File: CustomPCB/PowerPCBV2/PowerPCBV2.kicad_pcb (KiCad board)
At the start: 2 copper layers, 18 parts, among them J1 XT30, J2 XT60, J3 Barrel_Jack_12V, J4 Barrel_Jack_5V, U1 LM2677T-Fixed-12V, U2 LM2677T-Fixed-5V

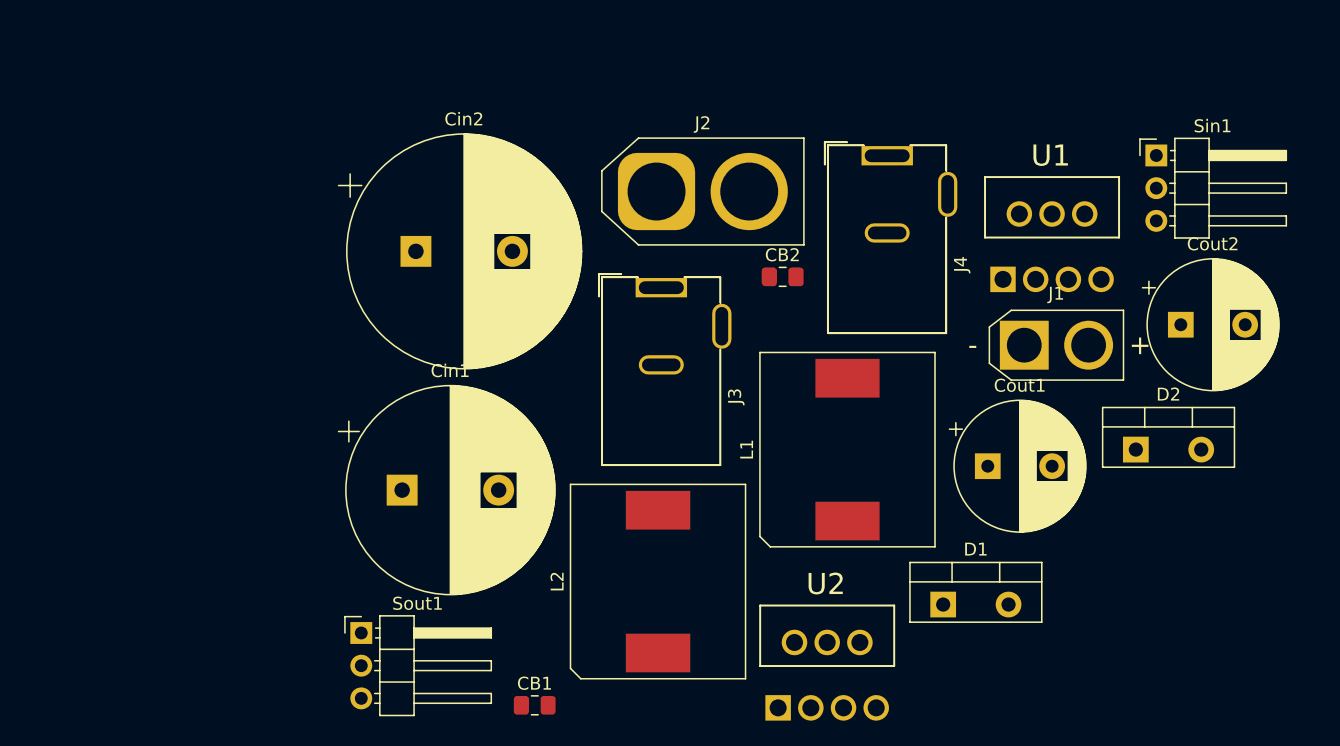
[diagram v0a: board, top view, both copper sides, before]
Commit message: update custom pcb and documentation
#23
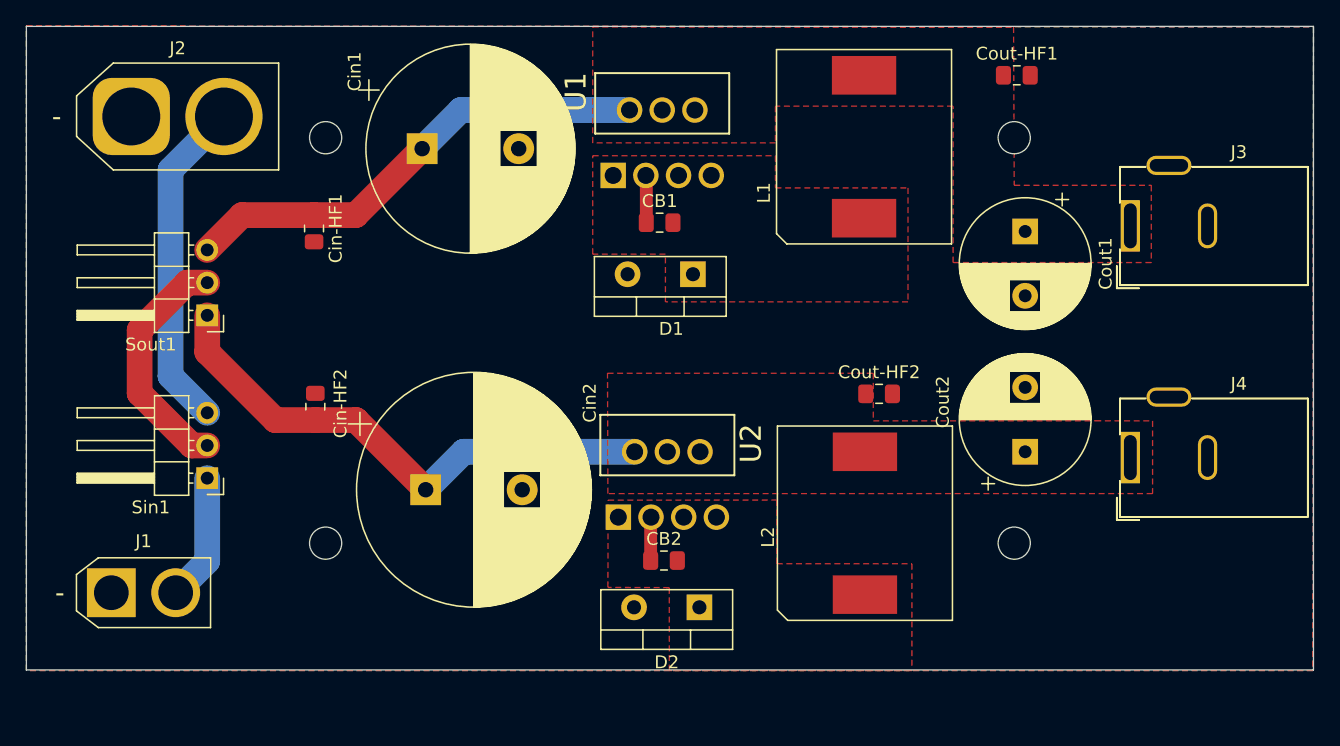
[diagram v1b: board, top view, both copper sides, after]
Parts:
- added Cin-HF1: 0.47uF, Capacitor_SMD:C_0805_2012Metric_Pad1.18x1.45mm_HandSolder, F.Cu at (92.3, 73.0)
- added Cin-HF2: 0.47uF, Capacitor_SMD:C_0805_2012Metric_Pad1.18x1.45mm_HandSolder, F.Cu at (92.5, 86.8)
- added Cout-HF1: 0.47uF, Capacitor_SMD:C_0805_2012Metric_Pad1.18x1.45mm_HandSolder, F.Cu at (146.9, 61.0)
- added Cout-HF2: 0.47uF, Capacitor_SMD:C_0805_2012Metric_Pad1.18x1.45mm_HandSolder, F.Cu at (136.2, 85.8)
- added H1: MountingHole, MountingHole:MountingHole_2.5mm, F.Cu at (93.2, 65.9)
- added H2: MountingHole, MountingHole:MountingHole_2.5mm, F.Cu at (93.2, 97.4)
- added H3: MountingHole, MountingHole:MountingHole_2.5mm, F.Cu at (146.8, 65.9)
- added H4: MountingHole, MountingHole:MountingHole_2.5mm, F.Cu at (146.8, 97.4)
- moved Sin1 77.9 mm to (84.0, 92.3), turned to 180 degrees
- moved J1 73.5 mm to (76.6, 101.2)
- moved J2 41.2 mm to (78.2, 64.2)
- moved CB1 38.7 mm to (119.2, 72.5)
- moved J3 36.7 mm to (155.8, 72.8), turned to 90 degrees
- moved D2 36.1 mm to (122.3, 102.4), turned to 180 degrees
- moved D1 32.2 mm to (121.8, 76.5), turned to 180 degrees
- moved U1 31.3 mm to (123.2, 57.6)
- moved J4 30.1 mm to (155.8, 90.8), turned to 90 degrees
- moved Sout1 27.4 mm to (84.0, 79.7), turned to 180 degrees
- moved Cin1 26.6 mm to (100.8, 66.8)
- moved CB2 23.9 mm to (119.5, 98.8)
- moved L1 23.6 mm to (135.1, 66.6)
- moved U2 19.3 mm to (123.6, 84.2)
- moved Cin2 18.5 mm to (101.0, 93.2)
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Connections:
- U1 pad 5: GNDPWR -> unconnected-(U1-Pad5)
- U1 pad 7: GNDPWR -> unconnected-(U1-Pad7)
- U2 pad 5: GNDPWR -> unconnected-(U2-Pad5)
- U2 pad 7: GNDPWR -> unconnected-(U2-Pad7)
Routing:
- net Net-(Cin2-Pad1): track 0.00 -> 41.7 mm
- net Net-(Cin1-Pad1): track 0.00 -> 37.3 mm
- net Net-(J2-Pad2): track 0.00 -> 25.9 mm
- net Net-(Sin1-Pad2): track 0.00 -> 18.6 mm
- net Net-(J1-Pad2): track 0.00 -> 9.91 mm
- net Net-(CB1-Pad1): track 0.00 -> 3.68 mm
- net Net-(CB2-Pad1): track 0.00 -> 3.38 mm
- added copper zone on B.Cu, net GND
- added copper zone on F.Cu, net GND
- added copper zone on F.Cu, net Net-(CB1-Pad2)
- added copper zone on F.Cu, net Net-(CB2-Pad2)
- added copper zone on F.Cu, net Net-(Cout1-Pad1)
- added copper zone on F.Cu, net Net-(Cout2-Pad1)
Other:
- board outline added: 100 x 50 mm
